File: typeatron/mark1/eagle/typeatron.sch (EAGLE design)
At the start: 23 parts

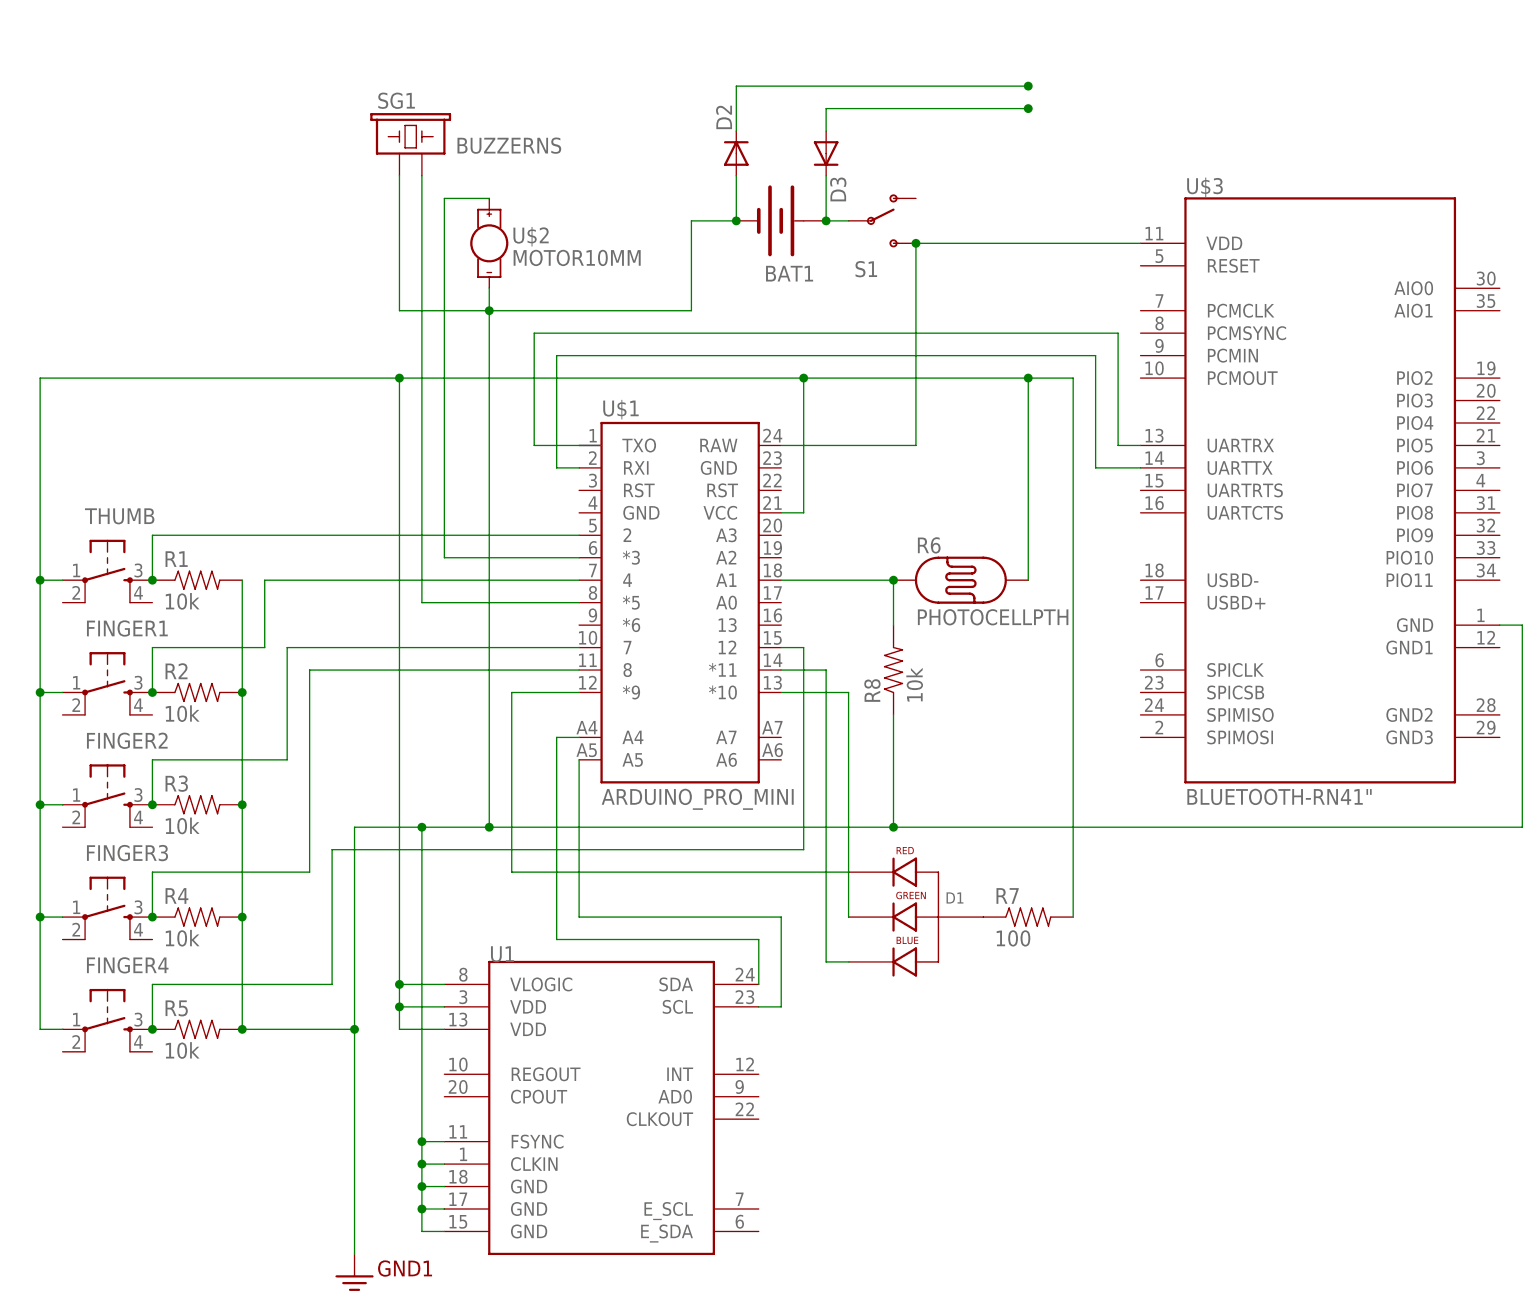
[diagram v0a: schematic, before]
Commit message: Moved Typeatron's protection diodes outside of the battery charger circuit, as the charger alternates current flow (presumably to charge and test)
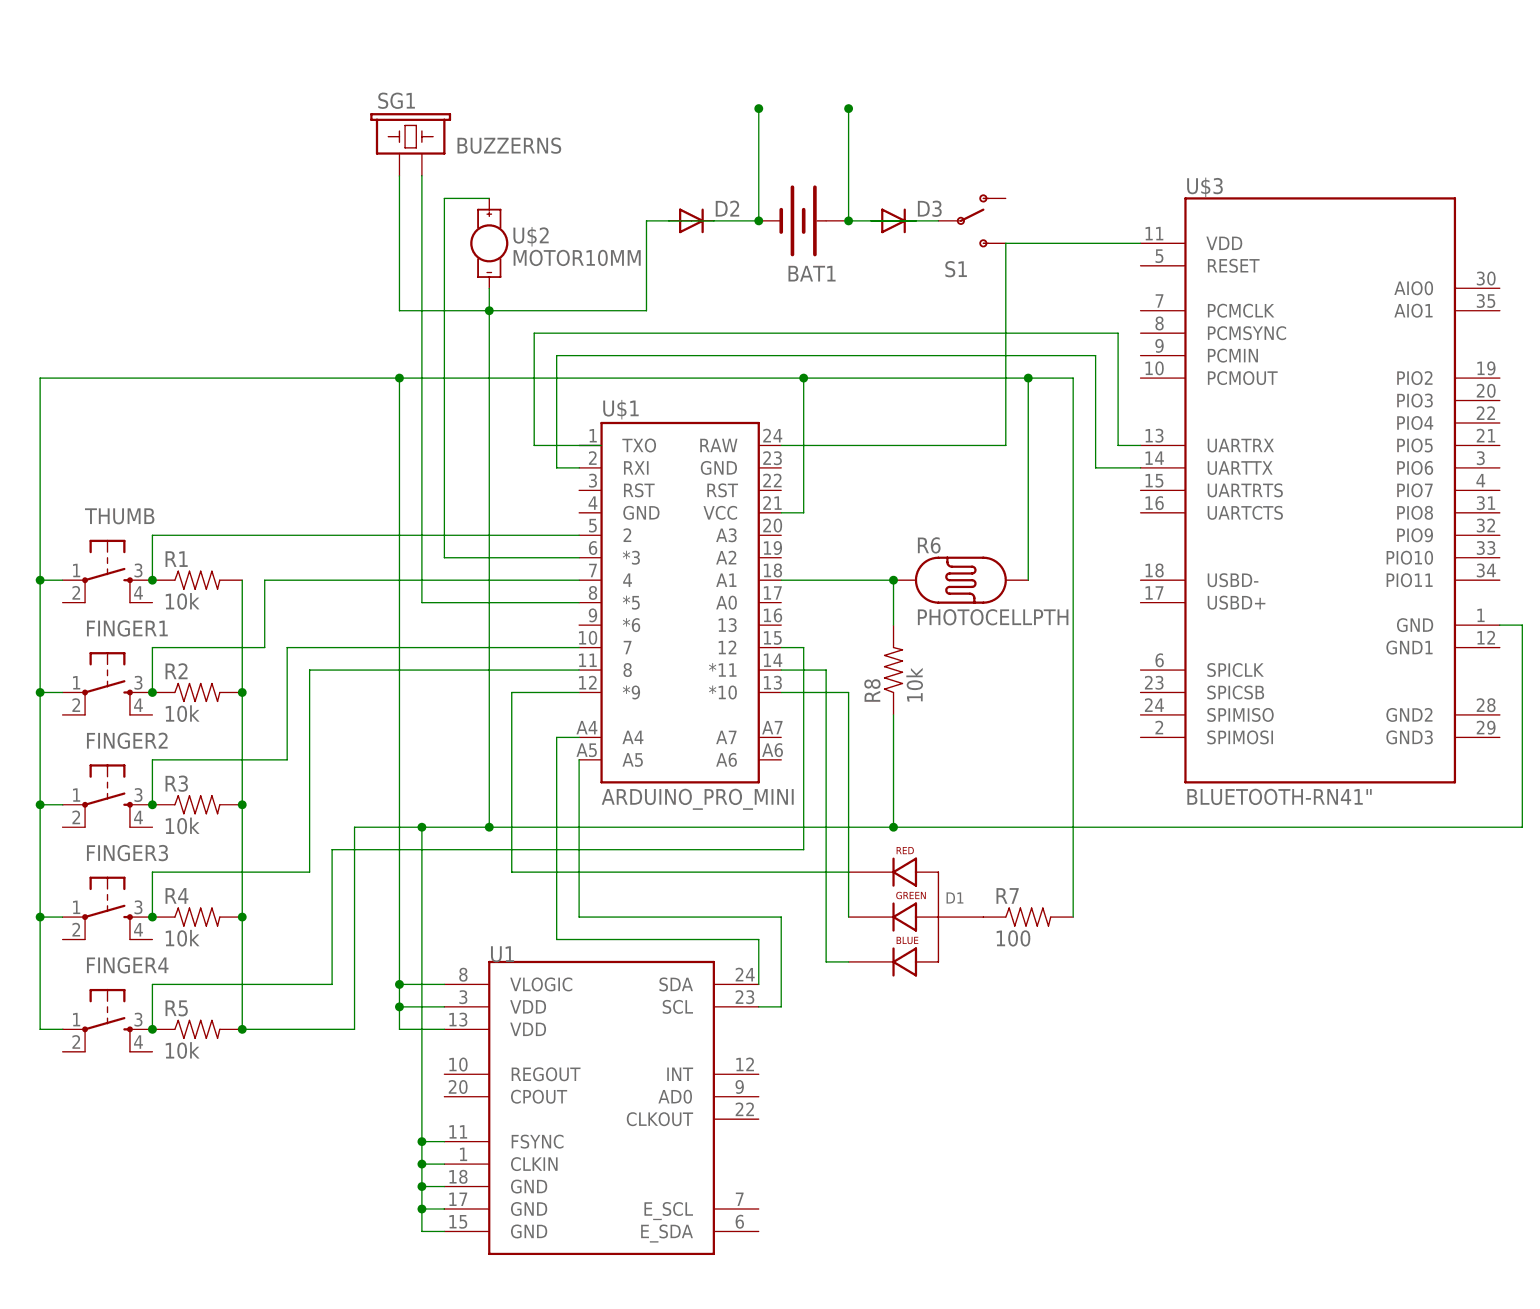
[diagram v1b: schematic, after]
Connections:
- removed net 3.3V: BAT1.-, D2.A, R1.2, R2.2, R3.2, R4.2, R5.2, R8.1, SG1.1, U$2.-, U$3.GND, U1.CLKIN, U1.FSYNC, U1.GND@15, U1.GND@17, U1.GND@18
- removed net CHARGE+: D3.A
- removed net CHARGE-: D2.C
- new net N$3: BAT1.-, D2.A, D2.C, R1.2, R2.2, R3.2, R4.2, R5.2, R8.1, SG1.1, U$2.-, U$3.GND, U1.CLKIN, U1.FSYNC, U1.GND@15, U1.GND@17, U1.GND@18
- net N$9: now also D3.A
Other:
- moved on the sheet: BAT1, D2, D3, S1
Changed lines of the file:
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@@
 <part name="R4" library="SparkFun-Resistors" deviceset="10KOHM1/6W5%(PTH)" device="KIT" value="10k"/>
 <part name="R5" library="SparkFun-Resistors" deviceset="10KOHM1/6W5%(PTH)" device="KIT" value="10k"/>
-<part name="GND1" library="SparkFun-Aesthetics" deviceset="GND2" device=""/>
 <part name="S1" library="SparkFun-Electromechanical" deviceset="SWITCH-SPDT" device="SMD2"/>
 <part name="SG1" library="SparkFun-Electromechanical" deviceset="BUZZER" device="NS"/>
@@
 <part name="U1" library="SparkFun-Sensors" deviceset="MPU-9150" device="QFN-24-NP"/>
 <part name="R8" library="SparkFun-Resistors" deviceset="10KOHM1/6W5%(PTH)" device="KIT" value="10k"/>
+<part name="D3" library="SparkFun-DiscreteSemi" deviceset="DIODE" device="PTH"/>
 <part name="D2" library="SparkFun-DiscreteSemi" deviceset="DIODE" device="PTH"/>
-<part name="D3" library="SparkFun-DiscreteSemi" deviceset="DIODE" device="PTH"/>
 </parts>
 <sheets>
@@
 <instance part="R4" gate="G$1" x="7.62" y="27.94"/>
 <instance part="R5" gate="G$1" x="7.62" y="15.24"/>
-<instance part="GND1" gate="G$1" x="25.4" y="-12.7"/>
-<instance part="S1" gate="1" x="83.82" y="106.68"/>
+<instance part="S1" gate="1" x="93.98" y="106.68"/>
 <instance part="SG1" gate="G$1" x="30.48" y="114.3"/>
 <instance part="U$2" gate="G$1" x="40.64" y="104.14"/>
 <instance part="U$3" gate="G$1" x="134.62" y="76.2"/>
-<instance part="BAT1" gate="G$1" x="73.66" y="106.68" rot="R180"/>
+<instance part="BAT1" gate="G$1" x="76.2" y="106.68" rot="R180"/>
 <instance part="R6" gate="G$1" x="93.98" y="66.04"/>
 <instance part="D1" gate="G$1" x="86.36" y="27.94"/>
@@
 <instance part="U1" gate="G$1" x="53.34" y="5.08"/>
 <instance part="R8" gate="G$1" x="86.36" y="55.88" rot="R90"/>
-<instance part="D2" gate="G$1" x="68.58" y="114.3" rot="R90"/>
-<instance part="D3" gate="G$1" x="78.74" y="114.3" rot="R270"/>
+<instance part="D3" gate="G$1" x="86.36" y="106.68"/>
+<instance part="D2" gate="G$1" x="63.5" y="106.68"/>
 </instances>
 <busses>
@@
 <pinref part="BAT1" gate="G$1" pin="+"/>
 <pinref part="S1" gate="1" pin="P"/>
-<wire x1="81.28" y1="106.68" x2="78.74" y2="106.68" width="0.1524" layer="91"/>
+<wire x1="88.9" y1="106.68" x2="81.28" y2="106.68" width="0.1524" layer="91"/>
+<wire x1="81.28" y1="119.38" x2="81.28" y2="106.68" width="0.1524" layer="91"/>
+<junction x="81.28" y="106.68"/>
+<pinref part="D3" gate="G$1" pin="A"/>
 <pinref part="D3" gate="G$1" pin="C"/>
-<wire x1="78.74" y1="111.76" x2="78.74" y2="106.68" width="0.1524" layer="91"/>
-<junction x="78.74" y="106.68"/>
+<wire x1="83.82" y1="106.68" x2="88.9" y2="106.68" width="0.1524" layer="91"/>
+<wire x1="88.9" y1="106.68" x2="91.44" y2="106.68" width="0.1524" layer="91"/>
+<junction x="81.28" y="119.38"/>
 </segment>
 </net>
@@
 <pinref part="S1" gate="1" pin="S"/>
 <pinref part="U$1" gate="G$1" pin="RAW"/>
-<wire x1="73.66" y1="81.28" x2="88.9" y2="81.28" width="0.1524" layer="91"/>
-<wire x1="88.9" y1="81.28" x2="88.9" y2="104.14" width="0.1524" layer="91"/>
-<wire x1="88.9" y1="104.14" x2="114.3" y2="104.14" width="0.1524" layer="91"/>
+<wire x1="73.66" y1="81.28" x2="99.06" y2="81.28" width="0.1524" layer="91"/>
+<wire x1="99.06" y1="81.28" x2="99.06" y2="104.14" width="0.1524" layer="91"/>
+<wire x1="99.06" y1="104.14" x2="114.3" y2="104.14" width="0.1524" layer="91"/>
 <pinref part="U$3" gate="G$1" pin="VDD"/>
-<junction x="88.9" y="104.14"/>
 </segment>
 </net>
@@
 </segment>
 </net>
-<net name="CHARGE+" class="0">
-<segment>
-<pinref part="D3" gate="G$1" pin="A"/>
-<wire x1="78.74" y1="116.84" x2="78.74" y2="119.38" width="0.1524" layer="91"/>
-<wire x1="78.74" y1="119.38" x2="101.6" y2="119.38" width="0.1524" layer="91"/>
-<junction x="101.6" y="119.38"/>
-</segment>
-</net>
-<net name="CHARGE-" class="0">
-<segment>
-<pinref part="D2" gate="G$1" pin="C"/>
-<wire x1="68.58" y1="116.84" x2="68.58" y2="121.92" width="0.1524" layer="91"/>
-<wire x1="68.58" y1="121.92" x2="101.6" y2="121.92" width="0.1524" layer="91"/>
-<junction x="101.6" y="121.92"/>
-</segment>
-</net>
 <net name="N$23" class="0">
 <segment>
@@
 </segment>
 </net>
-<net name="3.3V" class="0">
+<net name="N$3" class="0">
 <segment>
 <pinref part="U1" gate="G$1" pin="GND@15"/>
@@
 <wire x1="30.48" y1="111.76" x2="30.48" y2="96.52" width="0.1524" layer="91"/>
 <wire x1="30.48" y1="96.52" x2="40.64" y2="96.52" width="0.1524" layer="91"/>
-<wire x1="40.64" y1="96.52" x2="63.5" y2="96.52" width="0.1524" layer="91"/>
-<pinref part="D2" gate="G$1" pin="A"/>
+<wire x1="40.64" y1="96.52" x2="58.42" y2="96.52" width="0.1524" layer="91"/>
 <pinref part="BAT1" gate="G$1" pin="-"/>
-<wire x1="68.58" y1="111.76" x2="68.58" y2="106.68" width="0.1524" layer="91"/>
-<junction x="68.58" y="106.68"/>
-<wire x1="68.58" y1="106.68" x2="63.5" y2="106.68" width="0.1524" layer="91"/>
-<wire x1="63.5" y1="96.52" x2="63.5" y2="106.68" width="0.1524" layer="91"/>
+<wire x1="71.12" y1="119.38" x2="71.12" y2="106.68" width="0.1524" layer="91"/>
+<junction x="71.12" y="106.68"/>
+<wire x1="71.12" y1="106.68" x2="66.04" y2="106.68" width="0.1524" layer="91"/>
+<wire x1="66.04" y1="106.68" x2="60.96" y2="106.68" width="0.1524" layer="91"/>
+<wire x1="60.96" y1="106.68" x2="58.42" y2="106.68" width="0.1524" layer="91"/>
+<wire x1="58.42" y1="96.52" x2="58.42" y2="106.68" width="0.1524" layer="91"/>
 <junction x="40.64" y="96.52"/>
 <wire x1="157.48" y1="38.1" x2="157.48" y2="60.96" width="0.1524" layer="91"/>
@@
 <wire x1="33.02" y1="38.1" x2="25.4" y2="38.1" width="0.1524" layer="91"/>
 <wire x1="25.4" y1="38.1" x2="25.4" y2="15.24" width="0.1524" layer="91"/>
-<pinref part="GND1" gate="G$1" pin="3.3V"/>
 <junction x="33.02" y="38.1"/>
 <pinref part="R1" gate="G$1" pin="2"/>
-<wire x1="25.4" y1="15.24" x2="25.4" y2="-10.16" width="0.1524" layer="91"/>
 <wire x1="12.7" y1="66.04" x2="12.7" y2="53.34" width="0.1524" layer="91"/>
 <pinref part="R2" gate="G$1" pin="2"/>
@@
 <wire x1="12.7" y1="15.24" x2="25.4" y2="15.24" width="0.1524" layer="91"/>
 <junction x="12.7" y="15.24"/>
-<junction x="25.4" y="15.24"/>
-</segment>
-</net>
+<pinref part="D2" gate="G$1" pin="A"/>
+<pinref part="D2" gate="G$1" pin="C"/>
+<junction x="71.12" y="119.38"/>
+</segment>
+</net>

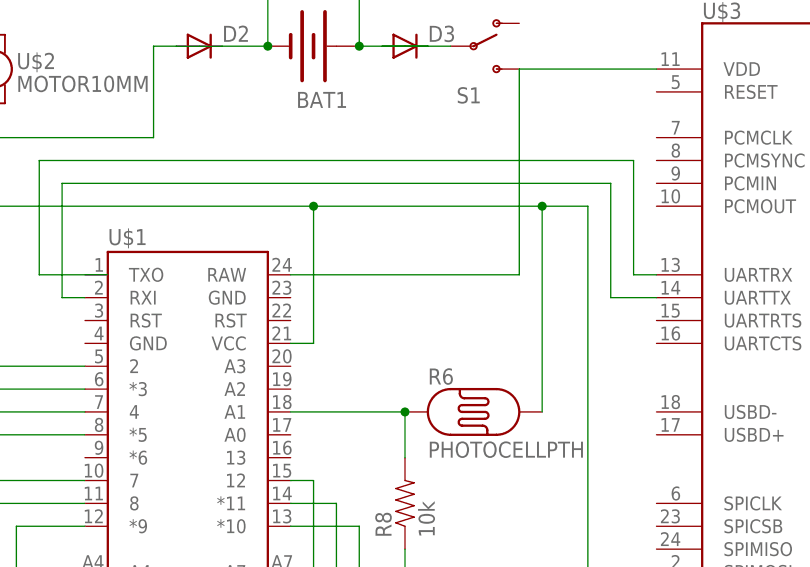
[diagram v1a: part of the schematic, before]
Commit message: Added one more diode to the Typeatron's power supply; prevents Arduino's VIN from powering the Bluetooth modem while in USB mode, interfering with programming
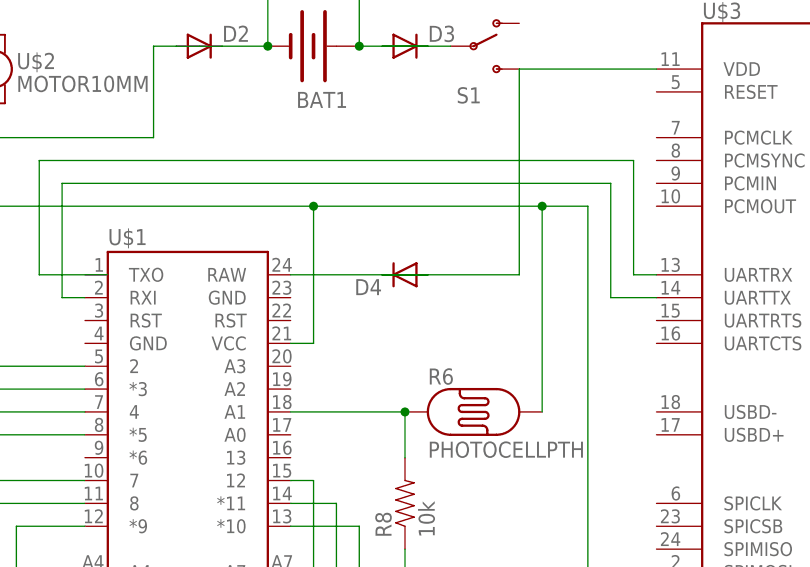
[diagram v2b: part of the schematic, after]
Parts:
- added D4: (no value), SparkFun-DiscreteSemi:DIODEPTH
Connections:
- net N$10: now also D4.A, D4.C
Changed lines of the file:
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@@
 <part name="D3" library="SparkFun-DiscreteSemi" deviceset="DIODE" device="PTH"/>
 <part name="D2" library="SparkFun-DiscreteSemi" deviceset="DIODE" device="PTH"/>
+<part name="D4" library="SparkFun-DiscreteSemi" deviceset="DIODE" device="PTH"/>
 </parts>
 <sheets>
@@
 <instance part="D3" gate="G$1" x="86.36" y="106.68"/>
 <instance part="D2" gate="G$1" x="63.5" y="106.68"/>
+<instance part="D4" gate="G$1" x="86.36" y="81.28" rot="R180"/>
 </instances>
 <busses>
@@
 <pinref part="S1" gate="1" pin="S"/>
 <pinref part="U$1" gate="G$1" pin="RAW"/>
-<wire x1="73.66" y1="81.28" x2="99.06" y2="81.28" width="0.1524" layer="91"/>
+<wire x1="73.66" y1="81.28" x2="88.9" y2="81.28" width="0.1524" layer="91"/>
+<wire x1="88.9" y1="81.28" x2="83.82" y2="81.28" width="0.1524" layer="91"/>
+<wire x1="83.82" y1="81.28" x2="99.06" y2="81.28" width="0.1524" layer="91"/>
 <wire x1="99.06" y1="81.28" x2="99.06" y2="104.14" width="0.1524" layer="91"/>
 <wire x1="99.06" y1="104.14" x2="114.3" y2="104.14" width="0.1524" layer="91"/>
 <pinref part="U$3" gate="G$1" pin="VDD"/>
-</segment>
-</net>
+<pinref part="D4" gate="G$1" pin="A"/>
+<pinref part="D4" gate="G$1" pin="C"/>
+</segment>
+</net>
